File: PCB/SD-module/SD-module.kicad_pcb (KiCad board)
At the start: 2 copper layers, 30.8 x 41.9 mm, 15 parts, among them J1 Connector, K1 SD-106M, U1 SE5218, U2 TXB0104PWR

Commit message: More OCD
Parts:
- moved C1 17.1 mm to (123.0, 103.8)
- moved C2 8.79 mm to (129.9, 103.7)
- moved R1 4.88 mm to (139.6, 106.8), turned to 90 degrees
- moved C7 3.53 mm to (135.8, 108.8)
- moved C5 2.59 mm to (129.8, 106.8), turned to -90 degrees
- moved U2 2.13 mm to (134.7, 105.0)
- moved C6 1.90 mm to (132.8, 108.8)
- moved C4 1.26 mm to (125.7, 108.4), turned to 0 degrees
- moved C3 1.07 mm to (139.6, 103.7)
- moved U1 0.42 mm to (125.8, 104.4)
- renumbered C3 to C1, C4 to C3, C1 to C4, C6 to C5, C5 to C6, REF**2 to REF**3
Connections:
- K1 pad 10: (no net) -> unconnected-(K1-CD-Pad10)
- K1 pad 11: (no net) -> unconnected-(K1-WP-Pad11)
- K1 pad 12: (no net) -> GND
- K1 pad 13: (no net) -> GND
- K1 pad 9: (no net) -> unconnected-(K1-Pad9)
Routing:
- net 3V3: track 34.4 -> 26.9 mm, vias 2 -> 0
- net MISO: track 15.0 -> 7.64 mm
- net SCK: track 18.0 -> 10.9 mm
- net MOSI: track 14.9 -> 8.14 mm
- net GND: track 15.7 -> 22.2 mm, vias 3 -> 2
- net MISO_L: track 8.83 -> 13.4 mm
- net CS_L: track 15.3 -> 11.2 mm
- net SCLK_L: track 8.60 -> 10.9 mm
- net 5V_burgerDisk: track 22.0 -> 20.7 mm
- net OE: track 2.09 -> 2.81 mm
- net MOSI_L: track 9.80 -> 10.3 mm
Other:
- board text added: "SD module for 5V MCUs © Colin Leroy-Mira https://colino.net"
- board text removed: "SD module for 5V MCUs"

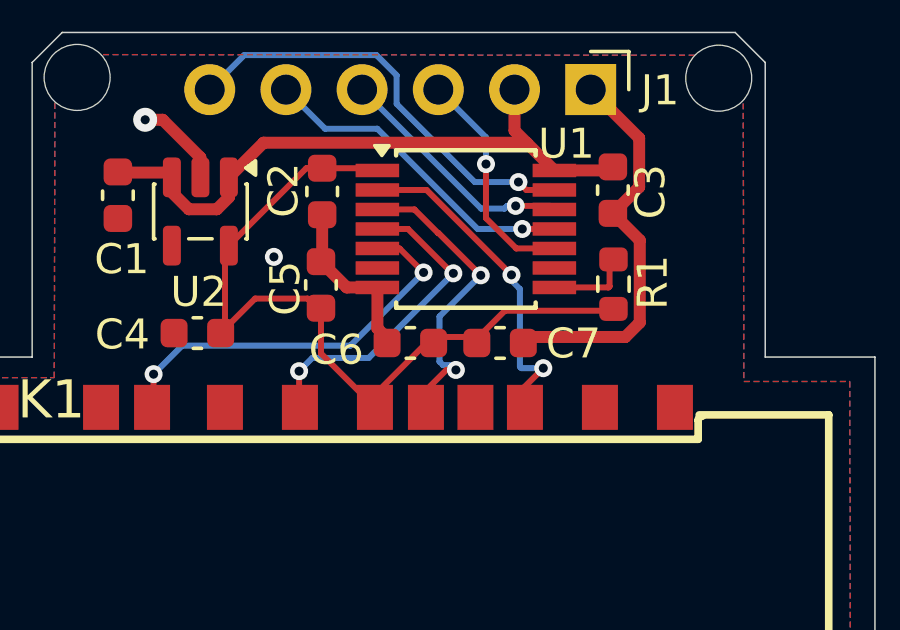
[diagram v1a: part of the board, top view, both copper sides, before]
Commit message: Fix microSD caps
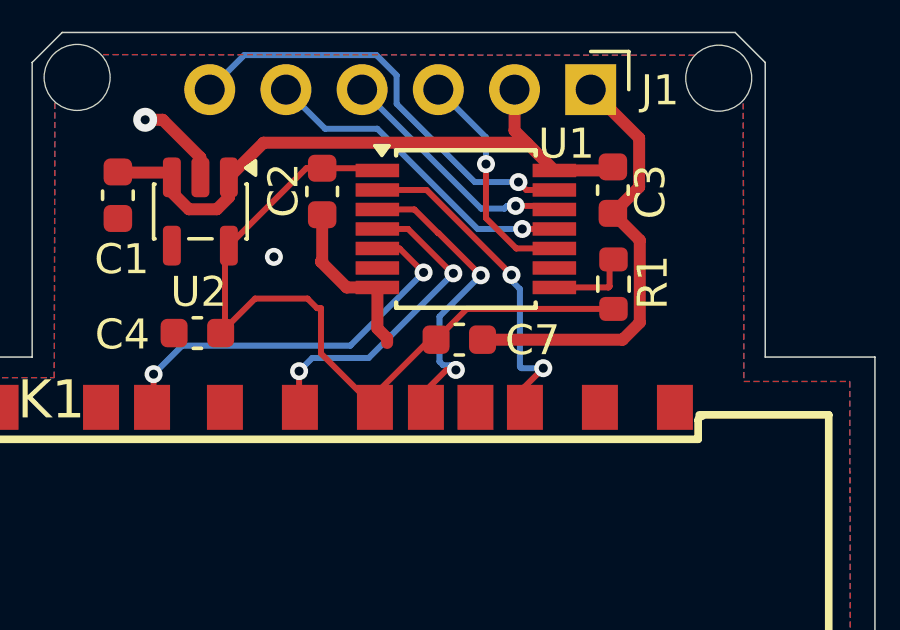
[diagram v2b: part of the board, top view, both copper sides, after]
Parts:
- removed C5: 2u2, Capacitor_SMD:C_0603_1608Metric
- removed C6: 100n, Capacitor_SMD:C_0603_1608Metric
- C7: value 100n -> 22uf
- moved C7 1.36 mm to (134.4, 108.6)
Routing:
- net GND: track 22.2 -> 23.5 mm

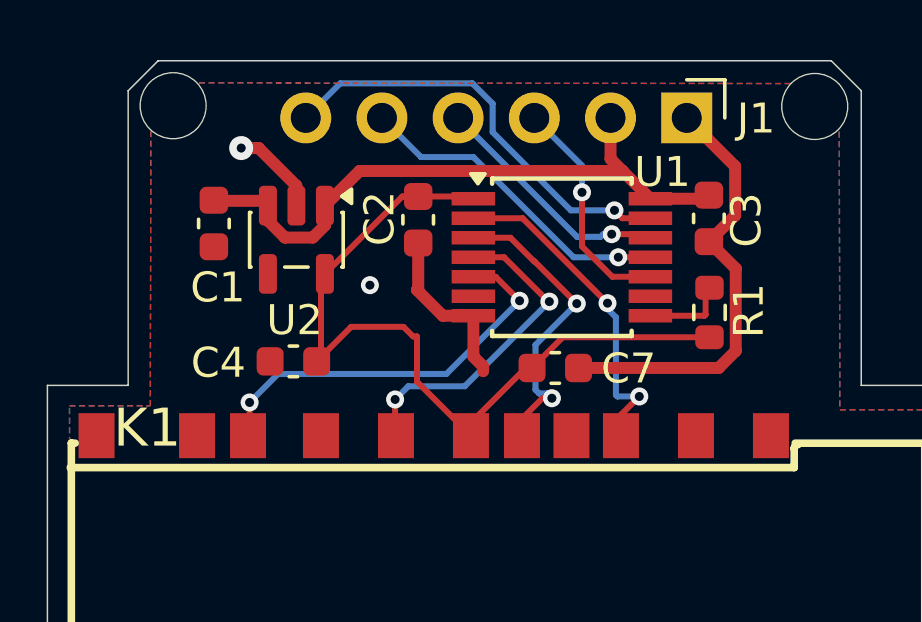
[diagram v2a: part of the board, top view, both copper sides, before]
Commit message: fatter traces
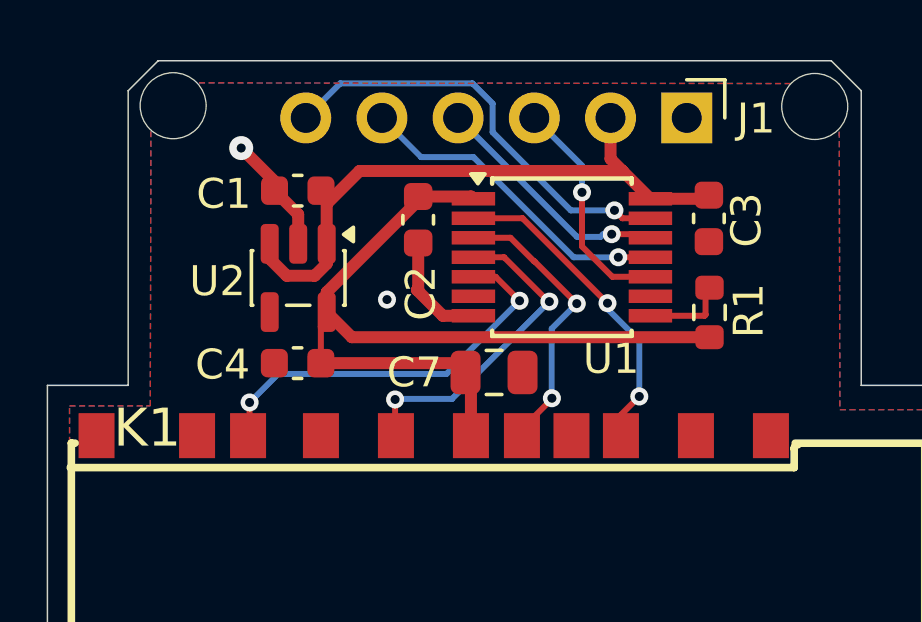
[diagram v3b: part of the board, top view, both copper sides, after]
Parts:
- C7: footprint Capacitor_SMD:C_0603_1608Metric -> Capacitor_SMD:C_0805_2012Metric
- moved C1 3.00 mm to (125.8, 102.7), turned to 0 degrees
- moved C7 2.05 mm to (132.4, 108.8)
- moved U1 1.27 mm to (125.9, 105.6)
- moved C4 0.15 mm to (125.8, 108.5)
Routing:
- net GND: track 23.5 -> 7.80 mm
- net 3V3: track 26.7 -> 29.0 mm
- net MOSI_L: track 10.3 -> 9.52 mm

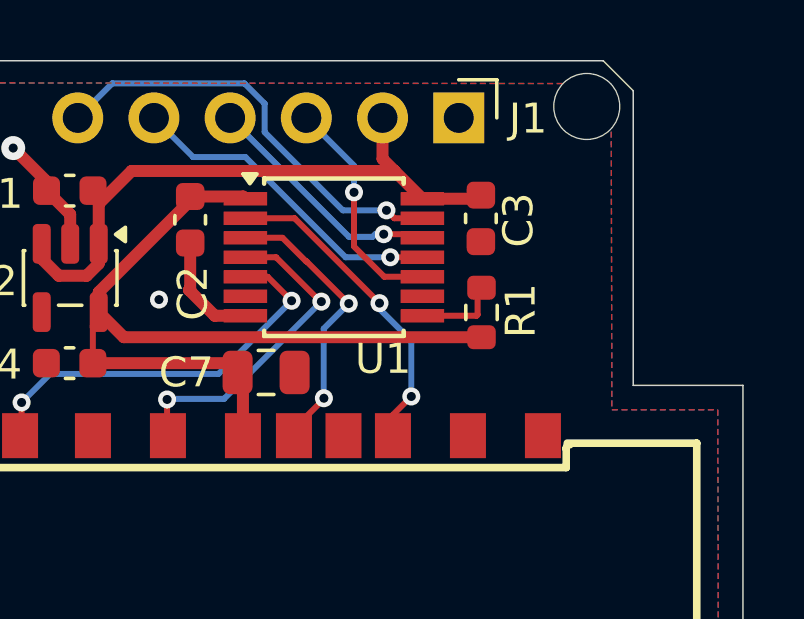
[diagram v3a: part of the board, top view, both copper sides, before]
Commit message: Enable teardrops
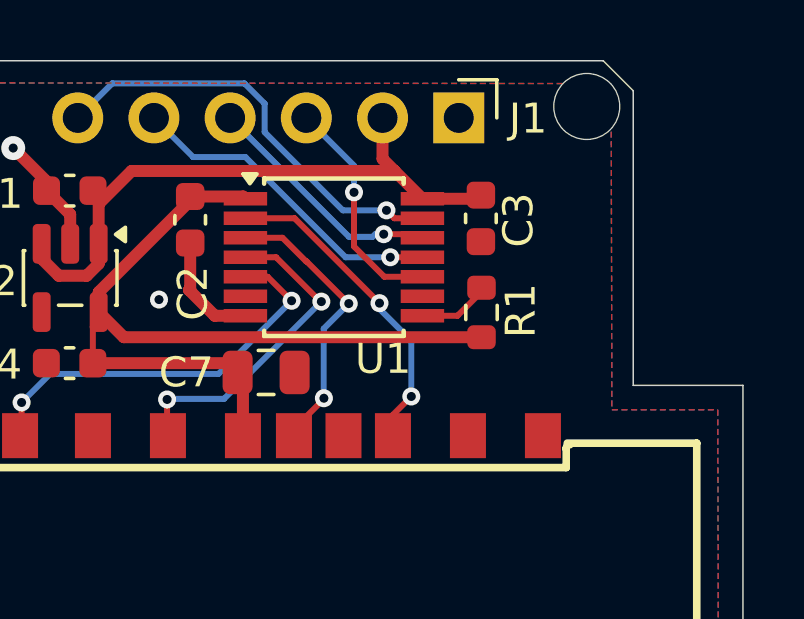
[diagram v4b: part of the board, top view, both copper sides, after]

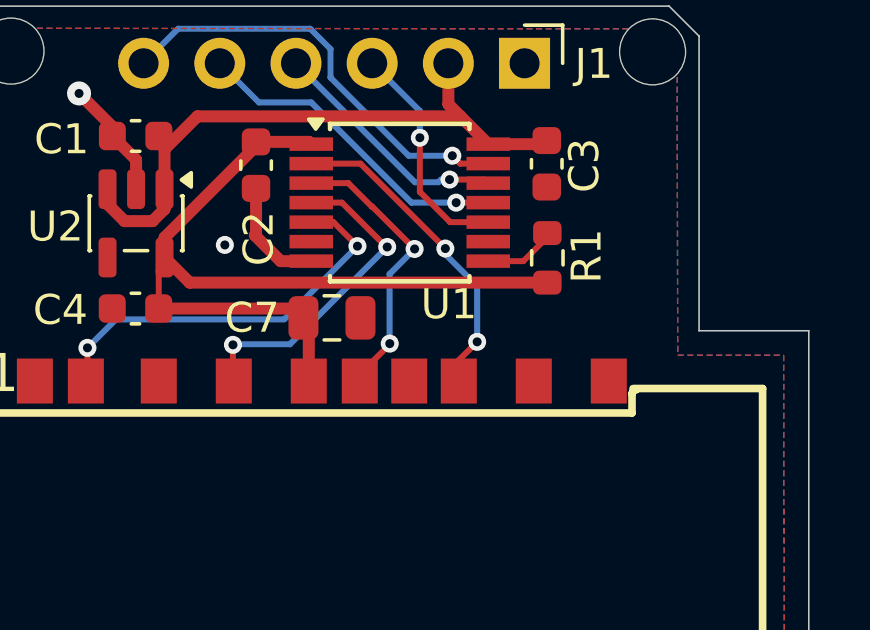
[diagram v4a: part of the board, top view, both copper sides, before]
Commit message: Fix SD module pins
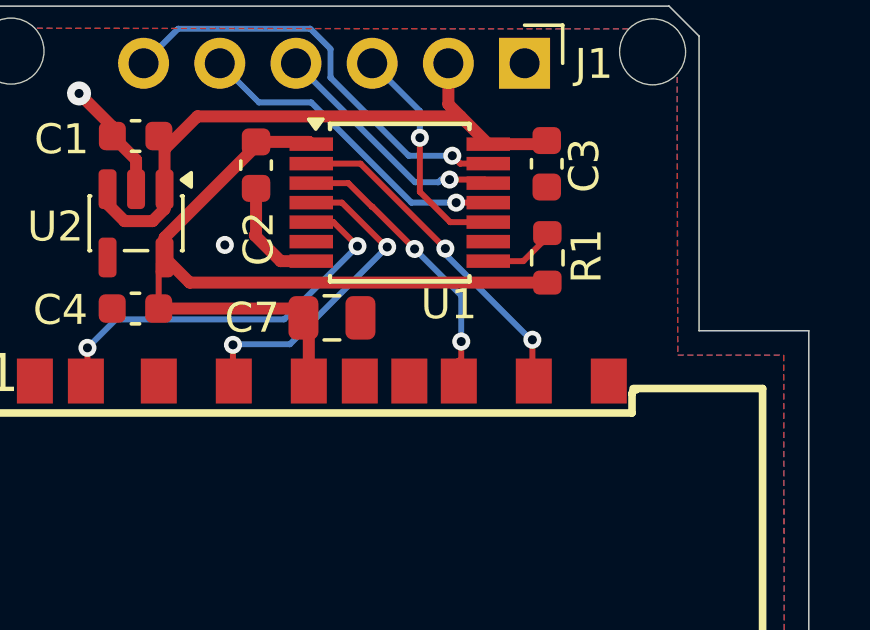
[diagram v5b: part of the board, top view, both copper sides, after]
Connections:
- K1 pad 1: unconnected-(K1-X-Pad1) -> CS_L
- K1 pad 2: CS_L -> MOSI_L
- K1 pad 3: MOSI_L -> GND
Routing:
- net MOSI_L: track 9.52 -> 10.2 mm
- net CS_L: track 10.8 -> 11.3 mm

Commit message: Update details
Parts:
- U1: value SE5218 -> SE5218ALG-LF
- moved U2 1.51 mm to (133.2, 104.7)
- moved C3 1.51 mm to (138.1, 103.4)
- moved R1 1.51 mm to (138.1, 106.5)
- moved C2 1.45 mm to (128.4, 104.0)
- moved C4 0.49 mm to (125.8, 108.0)
- moved U1 0.48 mm to (125.9, 105.2)
- moved C1 0.43 mm to (125.9, 102.3)
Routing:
- net GND: track 8.11 -> 4.43 mm, vias 2 -> 1
- net SCLK_L: track 10.9 -> 9.16 mm
- net MISO_L: track 13.4 -> 11.8 mm
- net SCK: track 10.9 -> 9.29 mm
- net CS_L: track 11.3 -> 12.8 mm
- net CS: track 14.4 -> 13.1 mm
- net MOSI: track 8.14 -> 6.99 mm
- net 3V3: track 29.0 -> 28.0 mm
- net 5V_burgerDisk: track 20.4 -> 19.4 mm
- net MISO: track 7.64 -> 6.73 mm
- net MOSI_L: track 10.2 -> 11.1 mm
